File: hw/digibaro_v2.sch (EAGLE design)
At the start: 11 parts

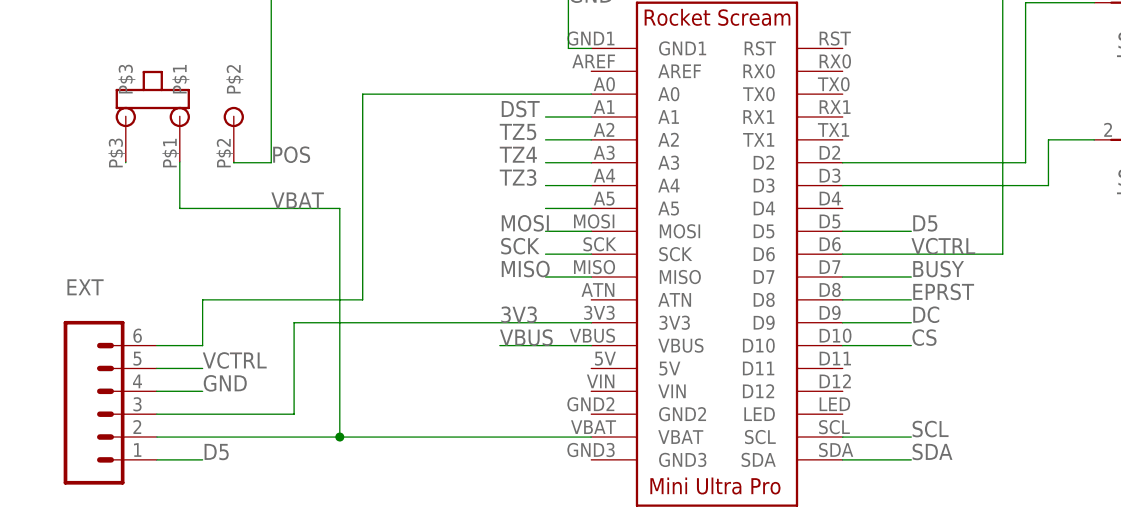
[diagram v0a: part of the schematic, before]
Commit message: fixed schematic, corrected footprint (switch + rocket scream) and improved layout
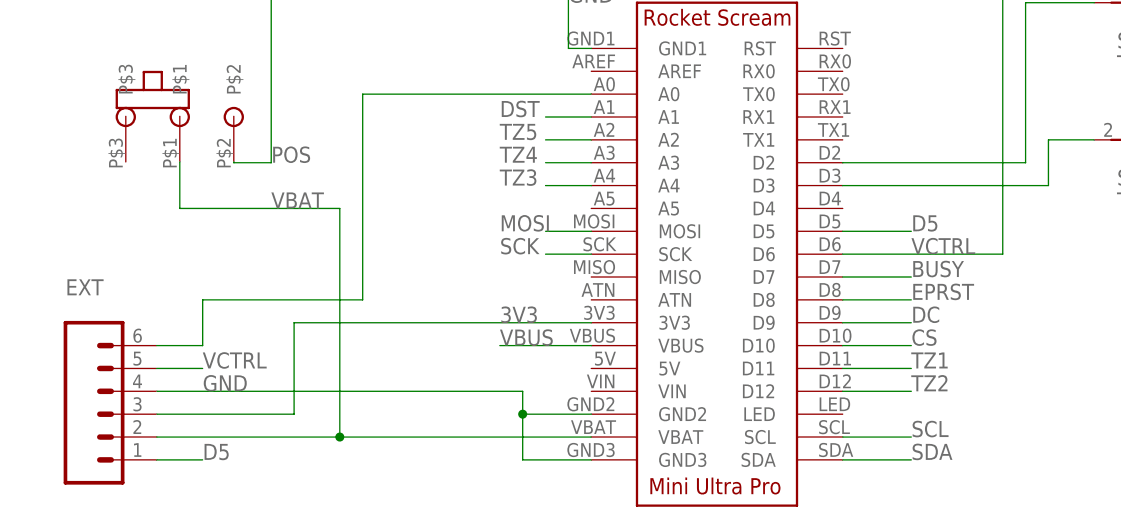
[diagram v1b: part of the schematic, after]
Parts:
- U$2: value SLIDE-SWITCHSS12SDH2 -> SLIDE-SWITCHNKKMINIATURE; device flupes:SLIDE-SWITCHSS12SDH2 -> flupes:SLIDE-SWITCHNKKMINIATURE
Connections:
- removed net MISO: U$3.MISO
- removed net N$14: U$2.P$3
- removed net N$5: U$3.A5
- net GND: now also U$3.GND2, U$3.GND3
- net TZ1: now also U$3.D11
- net TZ2: now also U$3.D12
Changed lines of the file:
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@@
 <part name="S3" library="switch-dil" library_urn="urn:adsk.eagle:library:375" deviceset="DA06" device="" package3d_urn="urn:adsk.eagle:package:27215/1"/>
 <part name="U$1" library="flupes" deviceset="BATTERY-HOLDER_3AA" device=""/>
-<part name="U$2" library="flupes" deviceset="SLIDE-SWITCH" device="SS12SDH2" value="SLIDE-SWITCHSS12SDH2"/>
+<part name="U$2" library="flupes" deviceset="SLIDE-SWITCH" device="NKKMINIATURE" value="SLIDE-SWITCHNKKMINIATURE"/>
 <part name="U$3" library="flupes" deviceset="ULTRA-MINI-PRO" device=""/>
 <part name="EXT" library="SparkFun-Connectors" library_urn="urn:adsk.eagle:library:513" deviceset="CONN_06" device="SILK_FEMALE_PTH" package3d_urn="urn:adsk.eagle:package:38009/1"/>
@@
 <segment>
 <pinref part="EXT" gate="G$1" pin="4"/>
-<wire x1="83.82" y1="38.1" x2="88.9" y2="38.1" width="0.1524" layer="91"/>
 <label x="88.9" y="38.1" size="1.778" layer="95"/>
+<wire x1="83.82" y1="38.1" x2="124.46" y2="38.1" width="0.1524" layer="91"/>
+<wire x1="124.46" y1="38.1" x2="124.46" y2="35.56" width="0.1524" layer="91"/>
+<pinref part="U$3" gate="G$1" pin="GND2"/>
+<wire x1="124.46" y1="35.56" x2="132.08" y2="35.56" width="0.1524" layer="91"/>
+<pinref part="U$3" gate="G$1" pin="GND3"/>
+<wire x1="132.08" y1="30.48" x2="124.46" y2="30.48" width="0.1524" layer="91"/>
+<wire x1="124.46" y1="30.48" x2="124.46" y2="35.56" width="0.1524" layer="91"/>
+<junction x="124.46" y="35.56"/>
 </segment>
 </net>
@@
 </segment>
 </net>
-<net name="N$14" class="0">
-<segment>
-<pinref part="U$2" gate="G$1" pin="P$3"/>
-<wire x1="80.36" y1="63.58" x2="80.36" y2="63.5" width="0.1524" layer="91"/>
-</segment>
-</net>
-<net name="MISO" class="0">
-<segment>
-<pinref part="U$3" gate="G$1" pin="MISO"/>
-<wire x1="132.08" y1="50.8" x2="127" y2="50.8" width="0.1524" layer="91"/>
-<label x="121.92" y="50.8" size="1.778" layer="95"/>
-</segment>
-</net>
 <net name="N$6" class="0">
 <segment>
@@
 <label x="144.78" y="88.9" size="1.778" layer="95"/>
 </segment>
+<segment>
+<pinref part="U$3" gate="G$1" pin="D11"/>
+<wire x1="160.02" y1="40.64" x2="167.64" y2="40.64" width="0.1524" layer="91"/>
+<label x="167.64" y="40.64" size="1.778" layer="95"/>
+</segment>
 </net>
 <net name="TZ2" class="0">
@@
 <wire x1="154.94" y1="91.44" x2="149.86" y2="91.44" width="0.1524" layer="91"/>
 <label x="144.78" y="91.44" size="1.778" layer="95"/>
+</segment>
+<segment>
+<pinref part="U$3" gate="G$1" pin="D12"/>
+<wire x1="160.02" y1="38.1" x2="167.64" y2="38.1" width="0.1524" layer="91"/>
+<label x="167.64" y="38.1" size="1.778" layer="95"/>
 </segment>
 </net>
@@
 </segment>
 </net>
-<net name="N$5" class="0">
-<segment>
-<pinref part="U$3" gate="G$1" pin="A5"/>
-<wire x1="132.08" y1="58.42" x2="127" y2="58.42" width="0.1524" layer="91"/>
-</segment>
-</net>
